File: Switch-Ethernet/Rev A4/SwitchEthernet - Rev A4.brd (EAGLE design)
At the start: 86 x 90 mm, 118 parts, among them J1 22-05-7028-02, P1 RB1-125BAG1A, T1 H1102FNL, T2 H1102FNL, U1 TC1264-3.3, U2 TC1264-1.8, U3 KSZ8995MA, U4 AT24C02C-SSHM-B, X1 NE8FAV, X2 NE8FAV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

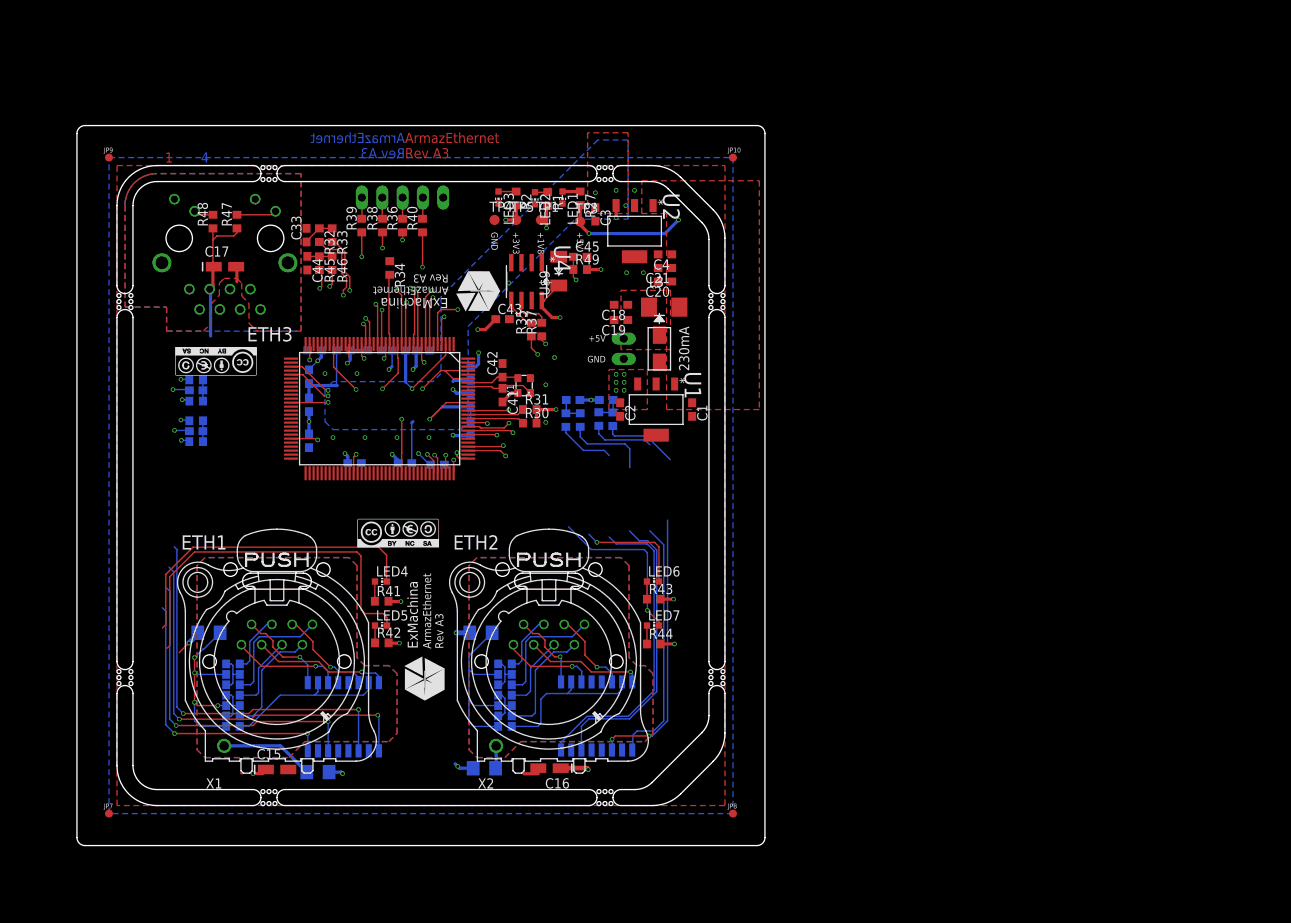
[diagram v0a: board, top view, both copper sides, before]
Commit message: Rename .sch and .brd
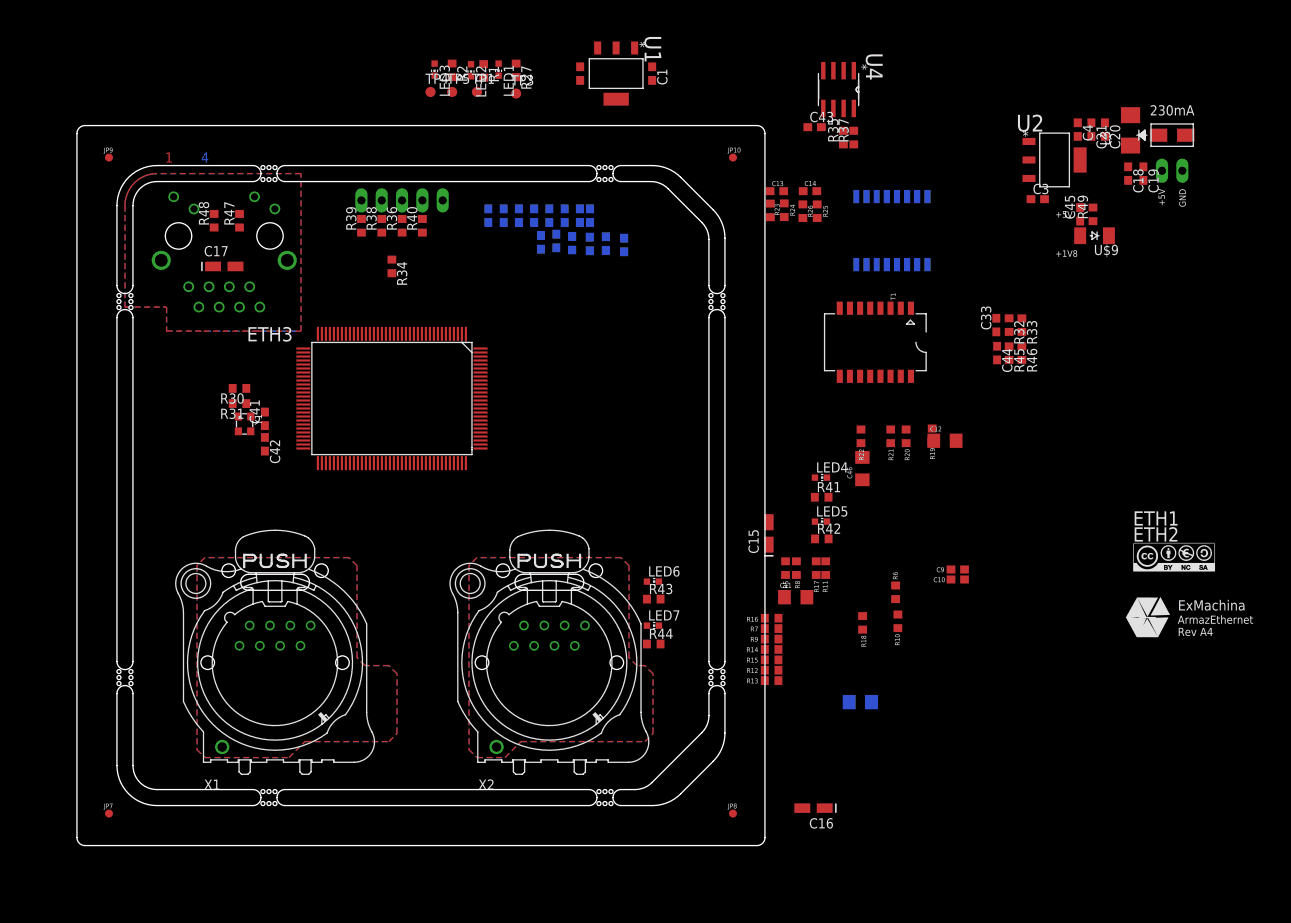
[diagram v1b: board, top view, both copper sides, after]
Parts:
- removed U$5: EXMACHINA-LOGO-NAME, exmachina:EXM-LOGO-BASELINE
- removed U$6: CC-BY-NC-SA, cc-by-sa:CC-BY-NC-SA
- moved C10 98.1 mm to (110.1, 33.3), flipped to the top
- moved U$7 97.0 mm to (137.1, 36.0)
- moved C9 96.8 mm to (110.1, 34.5), flipped to the top
- moved C12 95.1 mm to (108.5, 50.6), flipped to the top
- moved R19 92.0 mm to (106.9, 51.3), flipped to the top, turned to 90 degrees
- moved U$8 90.6 mm to (133.8, 28.5), turned to 0 degrees
- moved R20 88.8 mm to (103.6, 51.2), flipped to the top, turned to 90 degrees
- moved R21 87.1 mm to (101.7, 51.2), flipped to the top, turned to 90 degrees
- moved C33 86.9 mm to (114.9, 65.1)
- moved C44 86.9 mm to (115.0, 61.6)
- moved R32 86.9 mm to (116.5, 65.1)
- moved R33 86.9 mm to (118.1, 65.1)
- moved R45 86.9 mm to (116.5, 61.6)
- moved R46 86.9 mm to (118.1, 61.6)
- moved R6 84.5 mm to (102.3, 31.7), flipped to the top, turned to 90 degrees
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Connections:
- net L1-1: now also U3.103; no longer U3.98
- net L1-2: now also U3.102; no longer U3.97
- net L2-1: now also U3.98; no longer U3.106
- net L2-2: now also U3.97; no longer U3.105
- net L3-1: now also U3.106; no longer U3.103
- net L3-2: now also U3.105; no longer U3.102
- net RX1_ISO_N: now also U3.11; no longer U3.20
- net RX1_ISO_P: now also U3.10; no longer U3.19
- net RX2_ISO_N: now also U3.20; no longer U3.5
- net RX2_ISO_P: now also U3.19; no longer U3.4
- net RX3_ISO_N: now also U3.5; no longer U3.11
- net RX3_ISO_P: now also U3.4; no longer U3.10
- net TX1_ISO_N: now also U3.14; no longer U3.23
- net TX1_ISO_P: now also U3.13; no longer U3.22
- net TX2_ISO_N: now also U3.23; no longer U3.8
- net TX2_ISO_P: now also U3.22; no longer U3.7
- net TX3_ISO_N: now also U3.8; no longer U3.14
- net TX3_ISO_P: now also U3.7; no longer U3.13
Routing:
- net TX2_ISO_N: track 98.8 -> 0.00 mm, vias 3 -> 0
- net L1-2: track 96.0 -> 0.00 mm, vias 1 -> 0
- net +1V8: track 94.8 -> 0.00 mm, vias 14 -> 0
- net RX2_ISO_P: track 90.3 -> 0.00 mm, vias 1 -> 0
- net TX2_ISO_P: track 89.7 -> 0.00 mm, vias 1 -> 0
- net RX2_ISO_N: track 87.7 -> 0.00 mm, vias 1 -> 0
- net TX1_ISO_P: track 84.9 -> 0.00 mm, vias 4 -> 0
- net TX1_ISO_N: track 83.9 -> 0.00 mm, vias 4 -> 0
- net L1-1: track 79.8 -> 0.00 mm, vias 1 -> 0
- net RX1_ISO_P: track 75.6 -> 0.00 mm, vias 4 -> 0
- net RX1_ISO_N: track 69.5 -> 0.00 mm, vias 4 -> 0
- net L3-2: track 69.3 -> 0.00 mm, vias 1 -> 0
- net +3V3: track 64.3 -> 0.00 mm, vias 24 -> 0
- net L3-1: track 58.8 -> 0.00 mm, vias 1 -> 0
- net SDA: track 55.5 -> 0.00 mm, vias 4 -> 0
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- removed copper zone on layer 1, net +1V8
- removed copper zone on layer 16, net +1V8
- removed copper zone on layer 1, net +3V3
- removed copper zone on layer 16, net +3V3
- removed copper zone on layer 1, net +5V
- removed copper zone on layer 1, net GND
- removed copper zone on layer 15, net GND
- removed copper zone on layer 2, net GND
- removed copper zone on layer 1, net PW
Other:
- board text added: "ArmazEthernet Rev A4"
- board text removed: "+3V3"
- board text removed: "ArmazEthernet Rev A3"

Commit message: Preplace component on the board
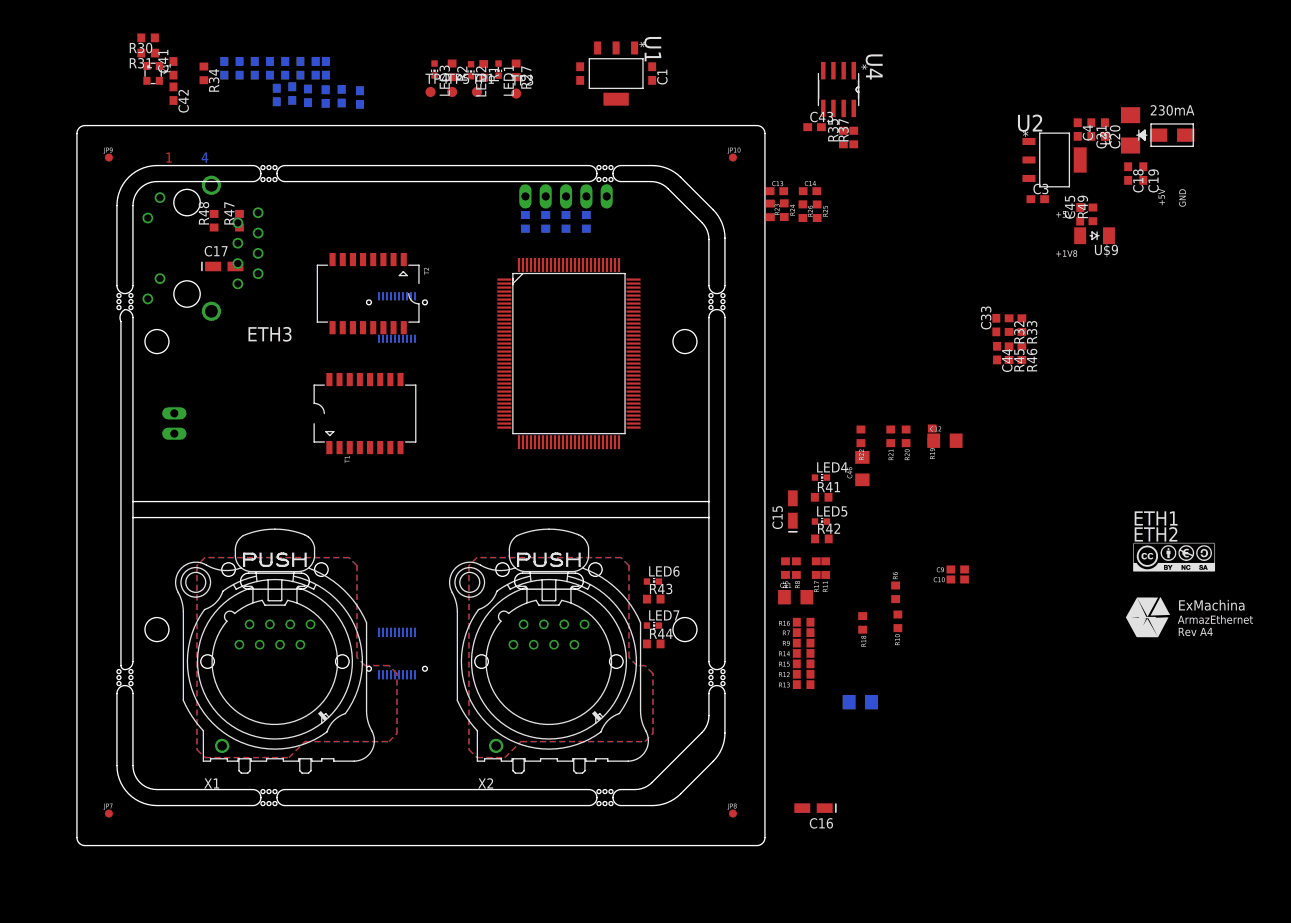
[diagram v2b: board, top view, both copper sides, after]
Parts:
- added J2: DF17(3.0)-20DP-0.5V(57), con-hirose:DF17-20DP
- added J3: (no value), con-hirose:DF17-20DS
- moved J1 128.7 mm to (12.2, 52.8), turned to 90 degrees
- moved T2 65.9 mm to (36.4, 69.0), flipped to the top
- moved T1 64.4 mm to (36.0, 54.0), turned to 0 degrees
- moved C42 45.3 mm to (12.1, 94.0)
- moved R30 45.3 mm to (8.89, 101.0)
- moved R31 45.3 mm to (8.89, 99.1)
- moved C41 45.3 mm to (12.1, 97.2)
- moved Y1 45.3 mm to (9.53, 96.5)
- moved C31 37.8 mm to (31.1, 97.2)
- moved C26 37.8 mm to (28.9, 93.7)
- moved C28 37.8 mm to (33.1, 93.7)
- moved C32 37.8 mm to (35.4, 93.5)
- moved C34 37.8 mm to (24.1, 97.2)
- moved C35 37.8 mm to (20.3, 97.2)
- moved C36 37.8 mm to (22.2, 97.2)
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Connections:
- net RX2_M renamed RX2_N
- net TX1_M renamed TX1_N
- net TX2_M renamed TX2_N
- removed net RX1_M: T1.9, X1.2
- new net CT_1: J2.7, J3.7, R6.2, T1.10, T1.15
- new net CT_2: J2.14, R13.2, T2.10, T2.15
- new net RX1_N: J2.3, J3.3, T1.9, X1.2
- net L1-1: now also J2.5, J3.5
- net L1-2: now also J2.6, J3.6
- net L2-1: now also J2.15, J2.16
- net N$1: now also J2.19; no longer R6.2, T1.10, T1.15
- net N$4: now also J2.18; no longer R13.2, T2.10, T2.15
- net RX1_P: now also J2.2, J3.2
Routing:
- removed copper zone on layer 1, net N$42
- removed copper zone on layer 16, net N$43
- removed copper zone on layer 15, net N$44
- removed copper zone on layer 2, net N$45
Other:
- outline, holes or cut-outs redrawn

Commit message: Connect board-to board connector
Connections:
- removed net N$1: J2.19
- removed net N$4: J2.18
- net +3V3: now also J2.1, J3.1
- net CT_1: now also J2.10, J3.10; no longer J2.7, J3.7
- net CT_2: now also J2.11, J3.11; no longer J2.14
- net GND: now also J2.14, J2.17, J2.20, J2.4, J2.7, J3.14, J3.17, J3.20, J3.4, J3.7
- net L1-1: now also J2.8, J3.8; no longer J2.5, J3.5
- net L1-2: now also J2.9, J3.9; no longer J2.6, J3.6
- net L2-1: now also J2.12, J2.13, J3.12, J3.13; no longer J2.15, J2.16
- net RX2_N: now also J2.15, J2.18, J3.15, J3.18
- net RX2_P: now also J2.16, J2.19, J3.16, J3.19
- net TX1_N: now also J2.6, J3.6
- net TX1_P: now also J2.5, J3.5

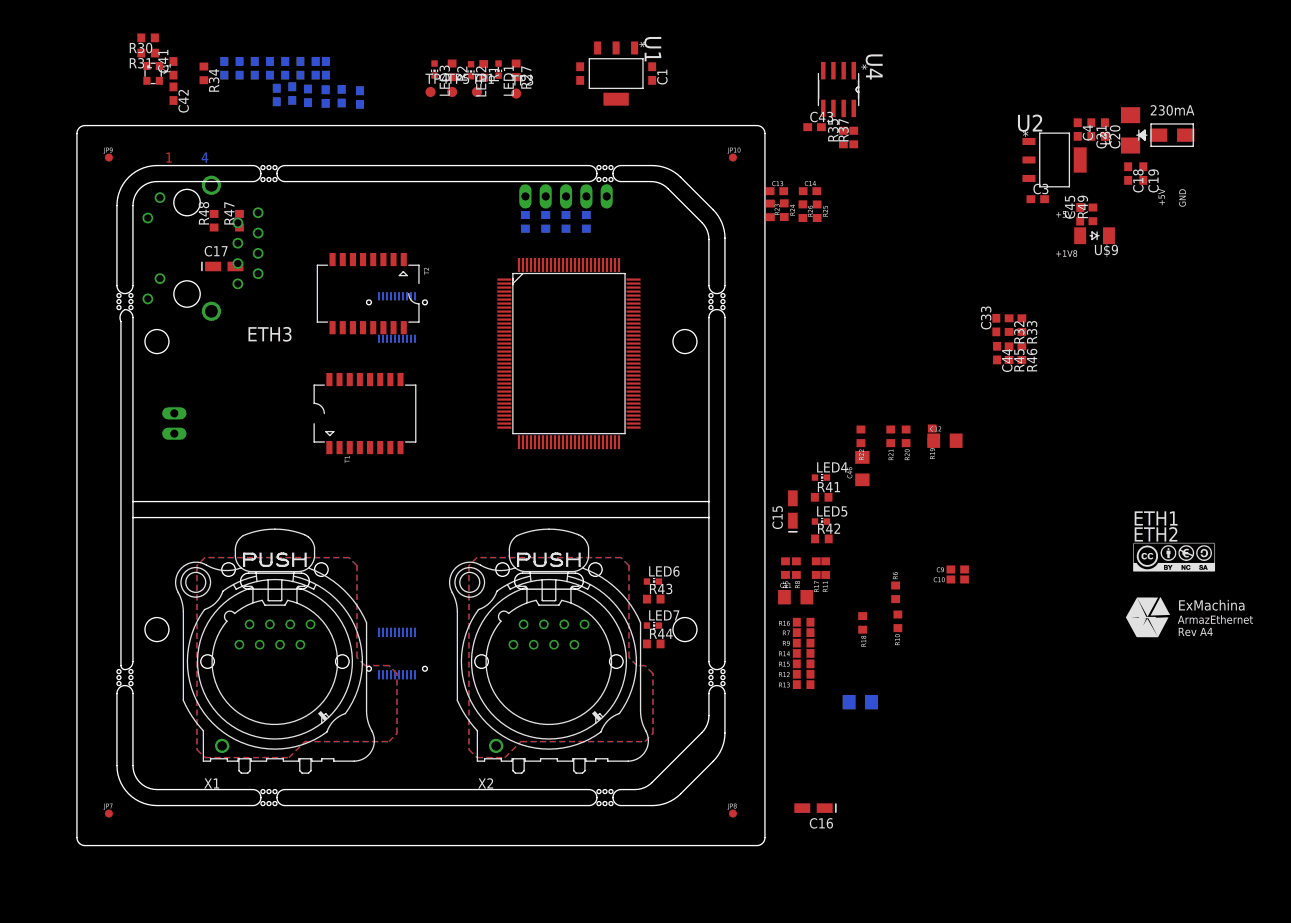
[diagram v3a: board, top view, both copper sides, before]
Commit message: Update connector and route eth 1,2 and 3
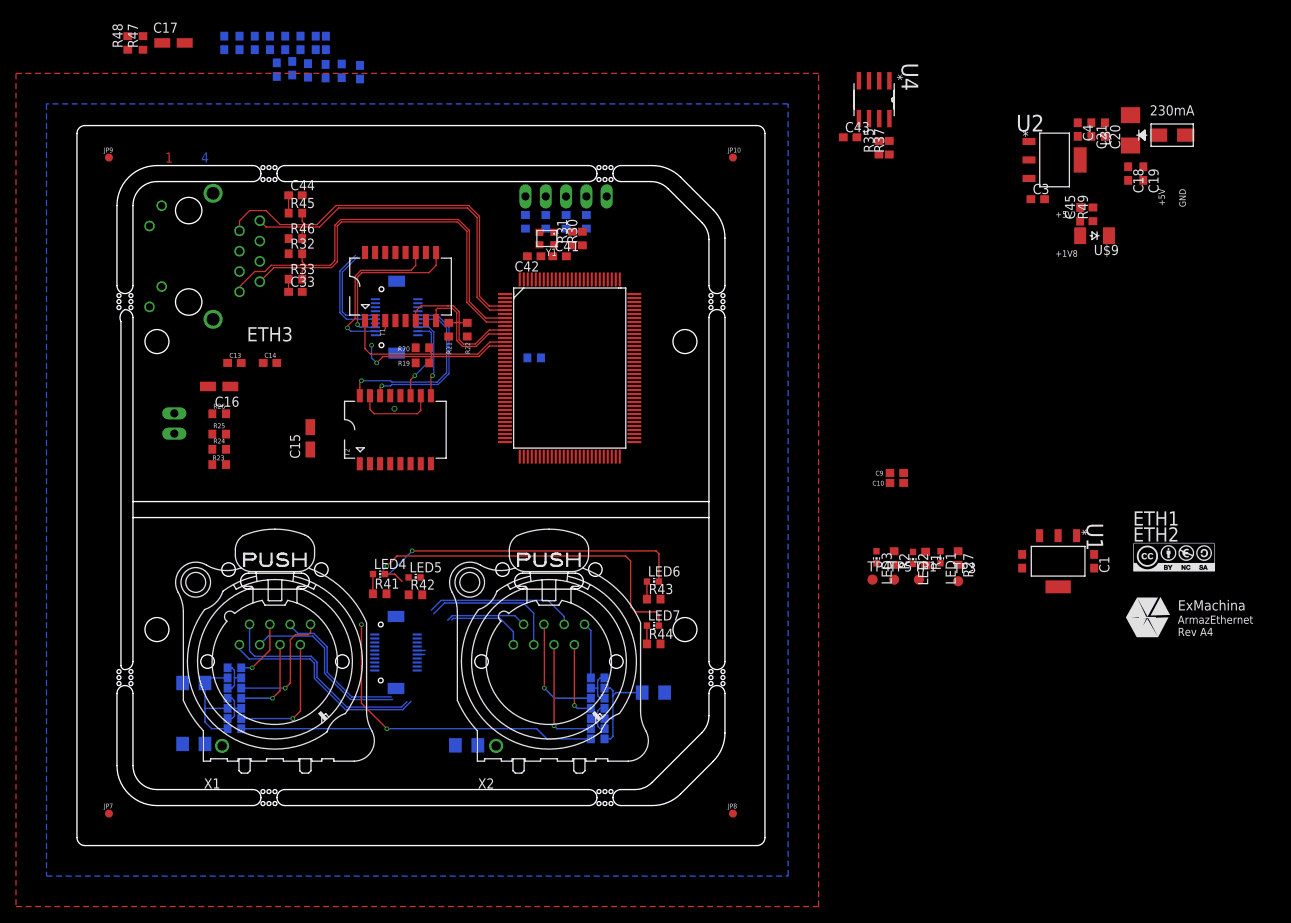
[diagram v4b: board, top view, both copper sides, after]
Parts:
- J2: value DF17(3.0)-20DP-0.5V(57) -> DF17(2.0)-20DP-0.5V(57)
- J3: value (none) -> DF17(4.0)-20DP-0.5V(57); device con-hirose:DF17-20DS -> con-hirose:DF17-20DP
- moved C12 98.7 mm to (14.6, 20.3), flipped to the bottom
- moved R46 91.9 mm to (27.3, 75.9), turned to 0 degrees
- moved C16 91.1 mm to (17.8, 57.4)
- moved R33 91.0 mm to (27.3, 70.8), turned to 0 degrees
- moved R45 90.9 mm to (27.3, 79.1), turned to 0 degrees
- moved C46 90.4 mm to (14.6, 12.7), flipped to the bottom, turned to 0 degrees
- moved C44 89.9 mm to (27.3, 81.3), turned to 0 degrees
- moved R32 89.7 mm to (27.3, 74.0), turned to 0 degrees
- moved C33 87.7 mm to (27.3, 69.2), turned to 0 degrees
- moved R6 84.4 mm to (19.7, 14.6), flipped to the bottom, turned to 180 degrees
- moved R10 83.2 mm to (19.7, 21.0), flipped to the bottom, turned to 180 degrees
- moved R2 82.3 mm to (102.1, 35.9)
- moved R27 82.3 mm to (110.1, 35.9)
- moved C2 82.3 mm to (118.1, 35.5)
- moved TP1 82.3 mm to (105.2, 33.2)
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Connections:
- net CT_2: now also J2.20, J3.20; no longer J2.11, J3.11
- net GND: now also J2.11, J3.11; no longer J2.20, J3.20
- net L2-1: now also J2.18, J3.18; no longer J2.12, J2.13, J3.12, J3.13
- net L2-2: now also J2.19, J3.19
- net RX2_N: now also J2.13, J3.13; no longer J2.15, J2.18, J3.15, J3.18
- net RX2_P: now also J2.12, J3.12; no longer J2.16, J2.19, J3.16, J3.19
- net TX2_N: now also J2.16, J3.16
- net TX2_P: now also J2.15, J3.15
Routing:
- net TX3_ISO_P: track 0.00 -> 51.8 mm
- net CT_2: track 0.00 -> 50.7 mm, vias 0 -> 2
- net RX3_ISO_P: track 0.00 -> 49.4 mm
- net TX3_ISO_N: track 0.00 -> 48.4 mm
- net RX1_N: track 0.00 -> 47.7 mm, vias 0 -> 1
- net RX1_P: track 0.00 -> 47.0 mm, vias 0 -> 1
- net RX3_ISO_N: track 0.00 -> 44.7 mm
- net L2-2: track 0.00 -> 43.0 mm, vias 0 -> 1
- net TX2_P: track 0.00 -> 41.2 mm, vias 0 -> 1
- net TX2_N: track 0.00 -> 40.6 mm, vias 0 -> 1
- net L2-1: track 0.00 -> 38.9 mm, vias 0 -> 1
- net TX1_P: track 0.00 -> 34.9 mm
- net TX1_N: track 0.00 -> 30.3 mm
- net TX1_ISO_P: track 0.00 -> 22.9 mm
- net TX1_ISO_N: track 0.00 -> 21.4 mm, vias 0 -> 2
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- added copper zone on layer 15, net +3V3
- added copper zone on layer 1, net GND
- added copper zone on layer 16, net GND
- added copper zone on layer 2, net GND
- removed copper zone on layer 1, net N$24
- removed copper zone on layer 16, net N$24
- removed copper zone on layer 15, net N$26
- removed copper zone on layer 2, net N$26
- removed copper zone on layer 15, net N$38
- removed copper zone on layer 2, net N$38
- removed copper zone on layer 1, net N$39
- removed copper zone on layer 16, net N$39
